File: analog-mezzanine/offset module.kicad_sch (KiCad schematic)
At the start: 6 parts

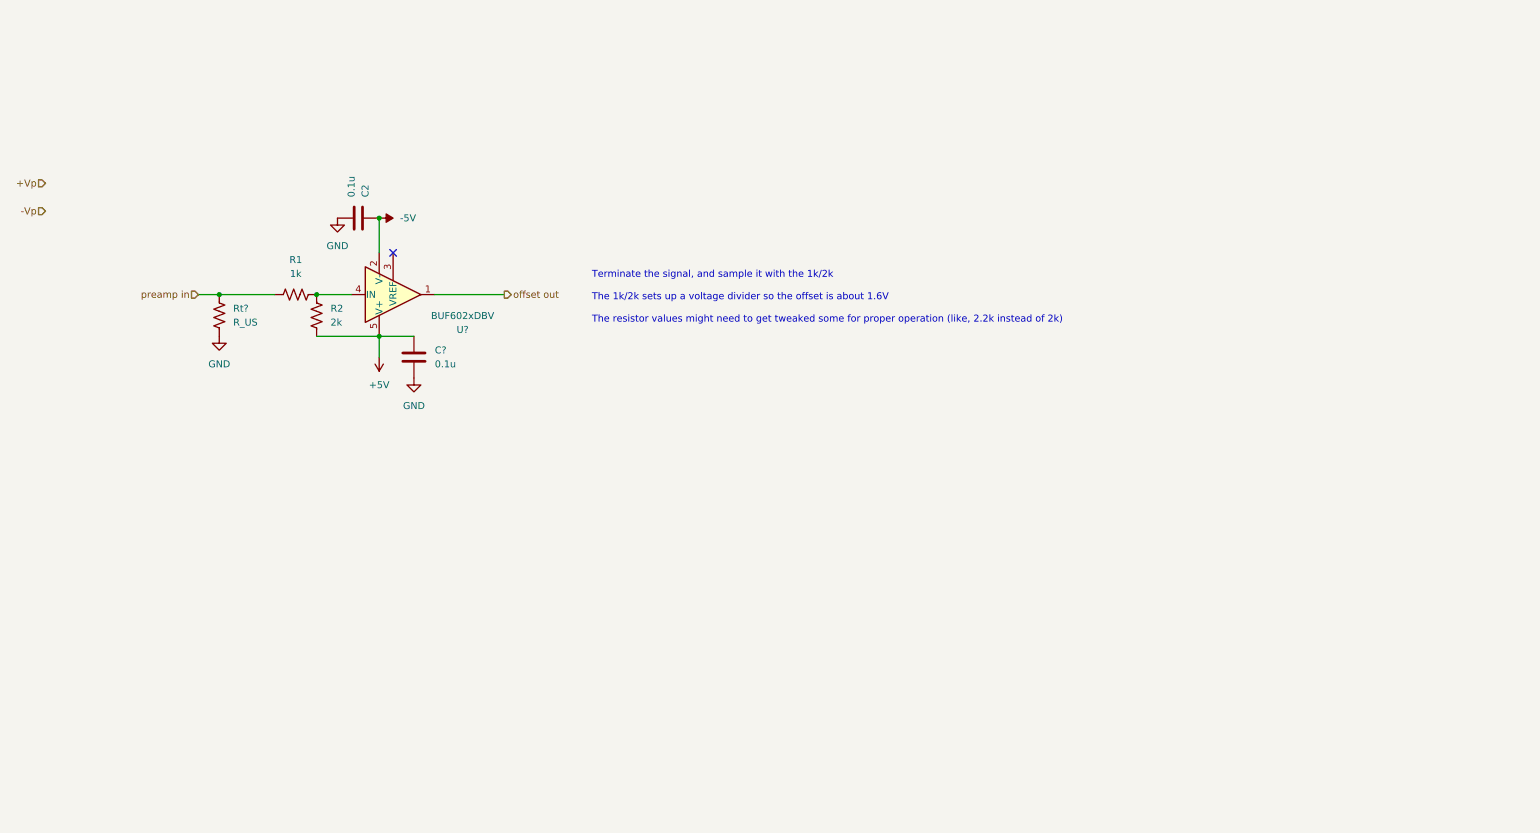
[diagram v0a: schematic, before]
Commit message: wire up linear regulators for offset
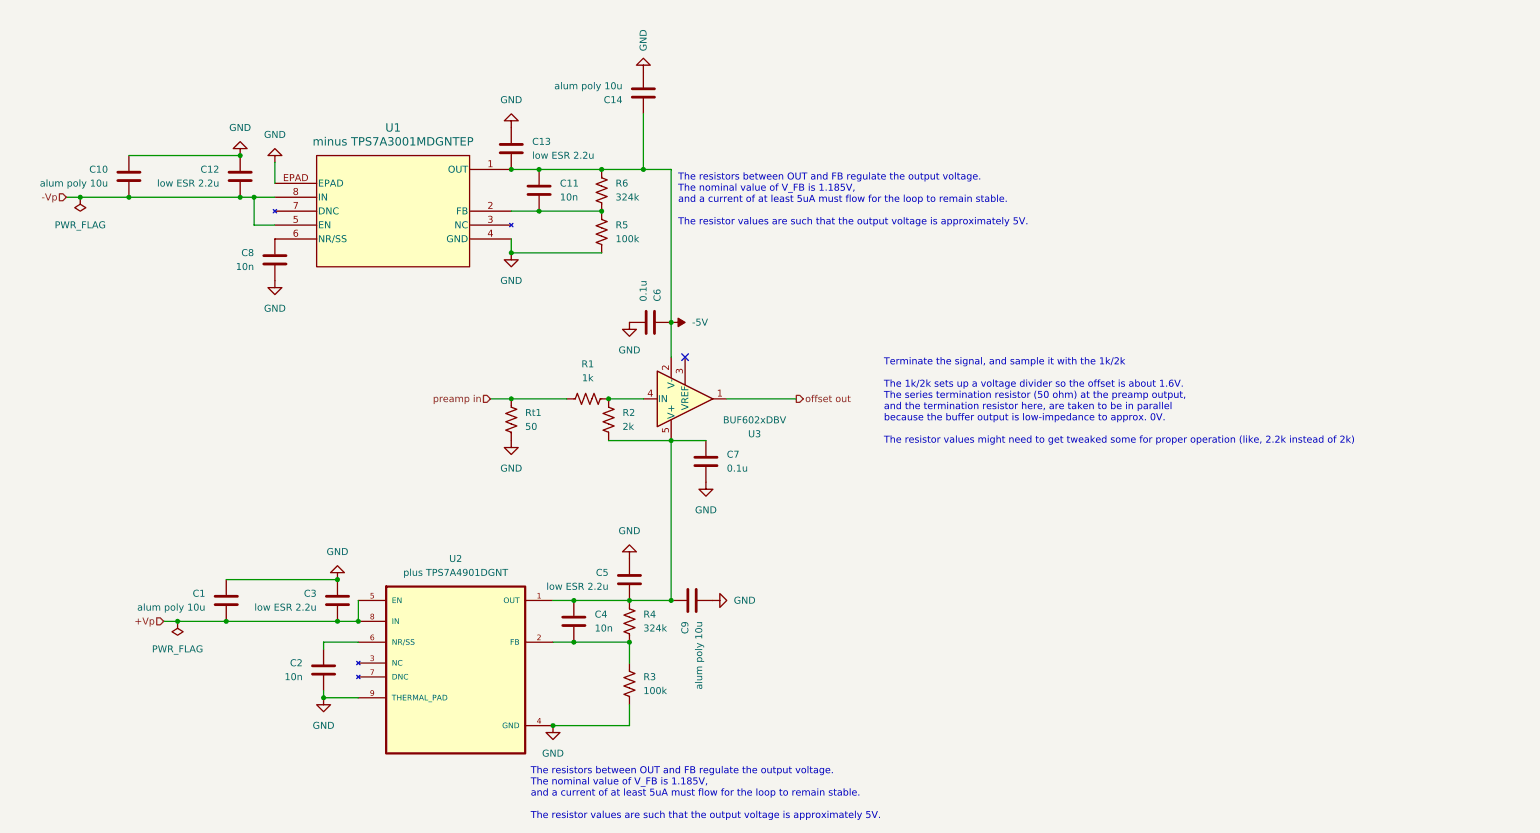
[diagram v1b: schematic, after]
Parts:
- added C1, C10, C14, C9: alum poly 10u, symbol Device:C
- added C11, C2, C4, C8: 10n, symbol Device:C
- added C12, C13, C3, C5: low ESR 2.2u, symbol Device:C
- added R3, R5: 100k, symbol Device:R_US
- added R4, R6: 324k, symbol Device:R_US
- added U1: minus TPS7A3001MDGNTEP, Library:DGN8_1P89X1P57, symbol Library:minus TPS7A3001MDGNTEP
- added U2: plus TPS7A4901DGNT, Library:SOP65P490X110-9N, symbol Library:plus TPS7A4901DGNT
- Rt1: renamed from Rt?; value R_US -> 50
- gave numbers to parts that had none: 2
- renumbered C2 to C6
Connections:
- net +Vp: now also C1.2, C3.2, U2.5 (EN), U2.8 (IN)
- net -5V: now also C11.1, C13.2, C14.1, R6.1, U1.1 (OUT)
- net -Vp: now also C10.2, C12.2, U1.5 (EN), U1.8 (IN)
- net GND: now also C1.1, C10.1, C12.1, C13.1, C14.2, C2.2, C3.1, C5.1, C8.2, C9.2, R3.2, R5.2, U1.4 (GND), U1.EPAD, U2.4 (GND), U2.9 (THERMAL_PAD)
- net +5V: no longer names the net of C7.2, R2.1, U3.5 (V+)
- net +5V: now also C4.1, C5.2, C9.1, R4.1, U2.1 (OUT)
- new net: C4.2, R3.1, R4.2, U2.2 (FB)
- new net: C11.2, R5.1, R6.2, U1.2 (FB)
- new net: C8.1, U1.6 (NR/SS)
- new net: C2.1, U2.6 (NR/SS)
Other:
- note added: "Terminate the signal, and sample it with the 1k/2k The 1k/2k sets up a voltage divider so the offset is about 1.6V. The series termination resistor (50 ohm) at the preamp output, and the termination resistor here, are taken to be in parallel because the buffer output is low-impedance to approx. 0V. The resistor values might need to get tweaked some for proper operation (like, 2.2k instead of 2k)"
- note added: "The resistors between OUT and FB regulate the output voltage. The nominal value of V_FB is 1.185V, and a current of at least 5uA must flow for the loop to remain stable. The resistor values are such that the output voltage is approximately 5V."
- note removed: "Terminate the signal, and sample it with the 1k/2k The 1k/2k sets up a voltage divider so the offset is about 1.6V The resistor values might need to get tweaked some for proper operation (like, 2.2k instead of 2k)"
- moved on the sheet: C6, C7, R1, R2, Rt1, U3

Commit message: start layout
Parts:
- removed C12, C13, C3: low ESR 2.2u, symbol Device:C
- removed C14: alum poly 10u, symbol Device:C
- removed C4: 10n, symbol Device:C
- removed R5: 100k, symbol Device:R_US
- removed R6: 324k, symbol Device:R_US
- added C13, C15, C3, C4: 10u alum poly, Capacitor_THT:CP_Radial_D8.0mm_P3.50mm, symbol Device:C_Polarized
- added C17: 0.01u, Capacitor_SMD:C_1206_3216Metric, symbol Device:C
- added C2: 200n, Capacitor_SMD:C_1206_3216Metric, symbol Device:C
- added C5: low ESR 2.2u, Capacitor_SMD:C_1206_3216Metric, symbol Device:C
- added C6: 10n, Capacitor_SMD:C_0805_2012Metric, symbol Device:C
- added L1, L2: 33u, Library:IND_VLS4015CX-330M-H, symbol Device:L
- added R2: 324k, Resistor_SMD:R_1206_3216Metric, symbol Device:R_US
- added R3: 100k, Resistor_SMD:R_1206_3216Metric, symbol Device:R_US
- added Rt2: 50, Resistor_SMD:R_0805_2012Metric, symbol Device:R_US
- C1: value alum poly 10u -> 200n; footprint (none) -> Capacitor_SMD:C_1206_3216Metric
- C10: value alum poly 10u -> 10n; footprint (none) -> Capacitor_SMD:C_0805_2012Metric
- C11: footprint (none) -> Capacitor_SMD:C_0805_2012Metric
- C12: renamed from C5; footprint (none) -> Capacitor_SMD:C_1206_3216Metric
- C7: renamed from C2; footprint (none) -> Capacitor_SMD:C_0805_2012Metric
- C8: value 10n -> low ESR 2.2u; footprint (none) -> Capacitor_SMD:C_1206_3216Metric
- C9: value alum poly 10u -> low ESR 2.2u; footprint (none) -> Capacitor_SMD:C_1206_3216Metric
- R5: renamed from R4; footprint (none) -> Resistor_SMD:R_1206_3216Metric
- R6: renamed from R3; footprint (none) -> Resistor_SMD:R_1206_3216Metric
- renumbered C6 to C14, C7 to C16, R2 to R4
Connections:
- net +Vp: now also C2.1, L2.1; no longer C1.2, U2.5 (EN), U2.8 (IN)
- net -Vp: now also C1.1, L1.1; no longer C10.2, U1.5 (EN), U1.8 (IN)
- net GND: now also C1.2, C8.1, C9.1, C13.1, C15.2, C2.2, C3.1, C4.2, C5.1, C6.2, R3.2; no longer C1.1, C10.1, C8.2, C9.2
- net offset out: now also Rt2.2; no longer U3.1
- net at R5.2, R6.1, U2.2 (FB): now also C11.2
- net at C12.2, C16.2, R4.1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: now also C11.1, C15.1, C17.1; no longer C9.1
- net at U1.2 (FB): now also C10.2, R2.2, R3.1; no longer C11.2
- net at U1.6 (NR/SS): now also C6.1; no longer C8.1
- net -5V: no longer names the net of C14.2, U1.1 (OUT), U3.2 (V-)
- net -5V: now also C10.1, C9.2, C13.2, C17.2, R2.1; no longer C11.1
- new net: C4.1, C8.2, L2.2, U2.5 (EN), U2.8 (IN)
- new net: C3.2, C5.2, L1.2, U1.5 (EN), U1.8 (IN)
- new net: Rt2.1, U3.1
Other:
- moved on the sheet: C12, C14, C16, C7, R1, R4, R5, R6, Rt1, U1, U2, U3

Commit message: laid out chunks and power
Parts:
- removed C13, C15, C3, C4: 10u alum poly, Capacitor_THT:CP_Radial_D8.0mm_P3.50mm, symbol Device:C_Polarized
- added C13, C15, C3, C4: low ESR 10u, Capacitor_SMD:C_1206_3216Metric, symbol Device:C
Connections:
- net GND: now also C13.1, C15.1, C3.1, C4.1
- net at C8.2, L2.2, U2.5 (EN)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: now also C4.2
- net at C10.1, C14.2, C17.2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: now also C13.2
- net at C5.2, L1.2, U1.5 (EN)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: now also C3.2
- net at C11.1, C12.2, C16.2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: now also C15.2

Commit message: re-layout, better ground plane config
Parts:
- removed C13, C15: low ESR 10u, Capacitor_SMD:C_1206_3216Metric, symbol Device:C
- renumbered C14 to C13, C16 to C14, C17 to C15
